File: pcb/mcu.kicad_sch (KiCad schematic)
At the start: 19 parts, among them J15 Conn_01x06_Pin, U20 TM4C123GH6PGEI7, Y2 Crystal_GND24

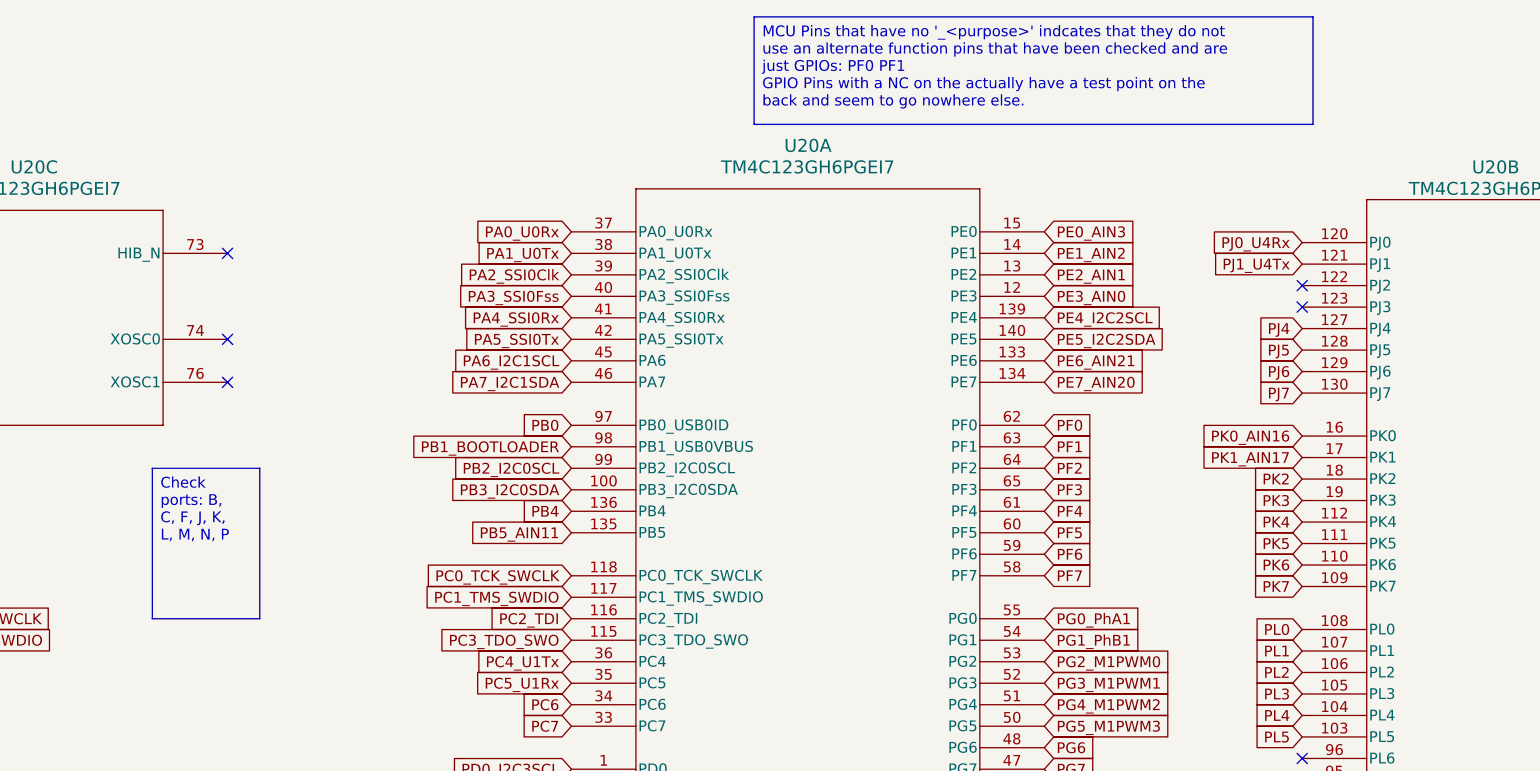
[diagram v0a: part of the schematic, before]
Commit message: Add the last few mystery components to the schematic, update the licence and start on RHSP
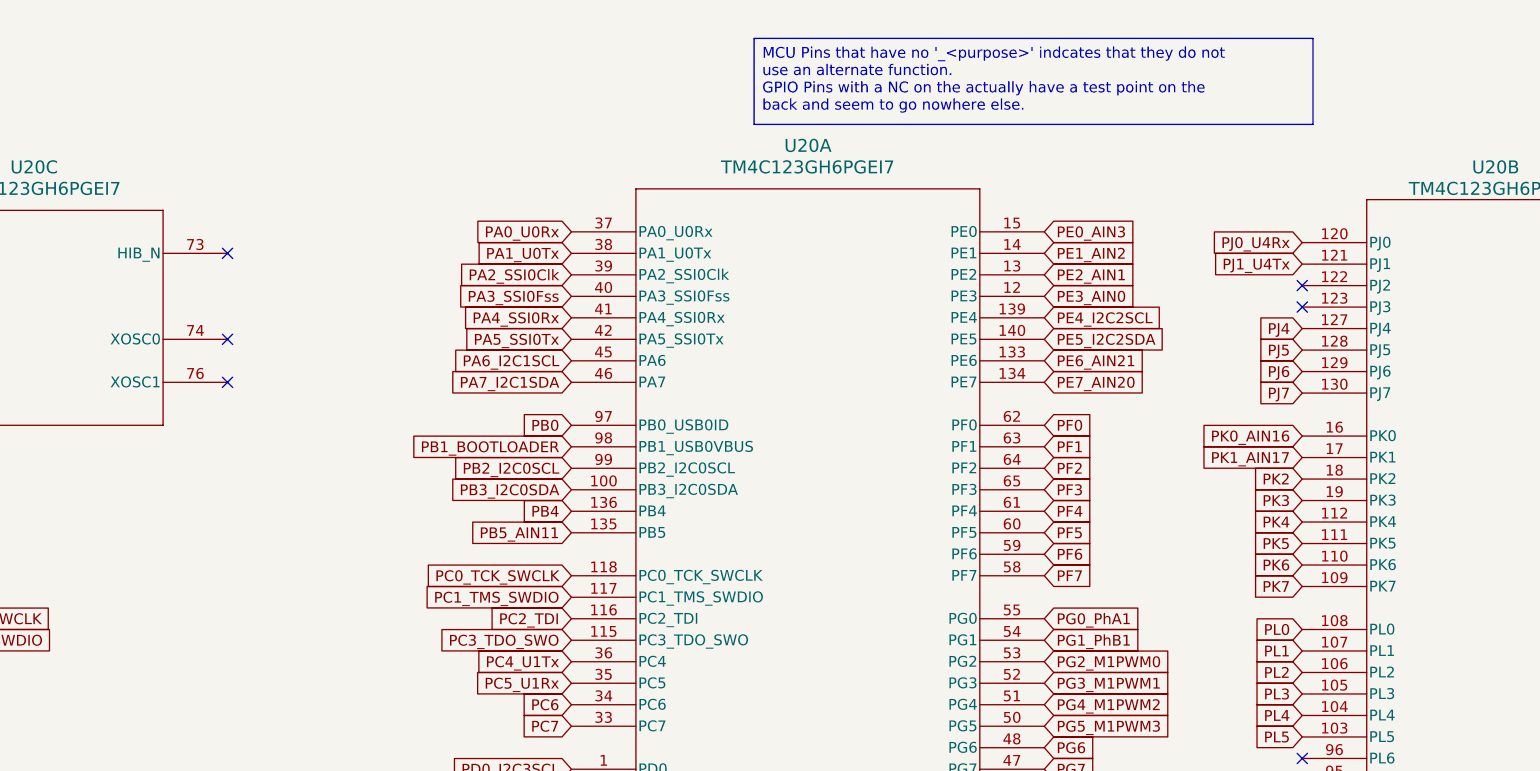
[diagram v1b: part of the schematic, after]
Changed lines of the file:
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@@
 		)
 	)
-	(text_box "MCU Pins that have no '_<purpose>' indcates that they do not use an alternate function pins that have been checked and are just GPIOs: PF0 PF1\nGPIO Pins with a NC on the actually have a test point on the back and seem to go nowhere else."
+	(text_box "MCU Pins that have no '_<purpose>' indcates that they do not use an alternate function.\nGPIO Pins with a NC on the actually have a test point on the back and seem to go nowhere else."
 		(exclude_from_sim no)
-		(at 149.86 2.54 0)
-		(size 66.04 12.7)
+		(at 149.86 5.08 0)
+		(size 66.04 10.16)
 		(margins 0.9525 0.9525 0.9525 0.9525)
 		(stroke
-			(width 0)
-			(type solid)
-		)
-		(fill
-			(type none)
-		)
-		(effects
-			(font
-				(size 1.27 1.27)
-			)
-			(justify left top)
-		)
-	)
-	(text_box "Check ports: B, C, F, J, K, L, M, N, P"
-		(exclude_from_sim no)
-		(at 78.74 55.88 0)
-		(size 12.7 17.78)
-		(margins 0.9525 0.9525 0.9525 0.9525)
-		(stroke

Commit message: Before tear out
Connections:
- net VCC: now also C49.1, U20.77 (VBAT)
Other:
- moved on the sheet: C49
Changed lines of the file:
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@@
 	)
 	(junction
+		(at 267.97 191.77)
+		(diameter 0)
+		(color 0 0 0 0)
+	)
+	(junction
 		(at 27.94 46.99)
 		(diameter 0)
@@
 	(wire
 		(pts
+			(xy 267.97 194.31) (xy 267.97 191.77)
+		)
+		(stroke
+			(width 0)
+			(type default)
+		)
+	)
+	(wire
+		(pts
 			(xy 214.63 152.4) (xy 215.9 152.4)
 		)
@@
 	(wire
 		(pts
+			(xy 280.67 194.31) (xy 278.13 194.31)
+		)
+		(stroke
+			(width 0)
+			(type default)
+		)
+	)
+	(wire
+		(pts
 			(xy 13.97 71.12) (xy 13.97 73.66)
 		)
@@
 	(wire
 		(pts
+			(xy 270.51 189.23) (xy 267.97 189.23)
+		)
+		(stroke
+			(width 0)
+			(type default)
+		)
+	)
+	(wire
+		(pts
 			(xy 45.72 76.2) (xy 27.94 76.2)
 		)
@@
 	(wire
 		(pts
+			(xy 267.97 194.31) (xy 270.51 194.31)
+		)
+		(stroke
+			(width 0)
+			(type default)
+		)
+	)
+	(wire
+		(pts
 			(xy 27.94 71.12) (xy 31.75 71.12)
 		)
@@
 	(wire
 		(pts
+			(xy 267.97 189.23) (xy 267.97 191.77)
+		)
+		(stroke
+			(width 0)
+			(type default)
+		)
+	)
+	(wire
+		(pts
 			(xy 214.63 166.37) (xy 222.25 166.37)
 		)
@@
 	(symbol
 		(lib_id "power:GND")
-		(at 275.59 191.77 90)
+		(at 280.67 194.31 90)
 		(unit 1)
 		(exclude_from_sim no)
@@
 		(fields_autoplaced yes)
 		(property "Reference" "#PWR093"
-			(at 281.94 191.77 0)
+			(at 287.02 194.31 0)
 			(effects
 				(font
@@
 		)
 		(property "Value" "GND"
-			(at 279.4 191.7699 90)
+			(at 284.48 194.3099 90)
 			(effects
 				(font
@@
 		)
 		(property "Footprint" ""
-			(at 275.59 191.77 0)
+			(at 280.67 194.31 0)
 			(effects
 				(font
@@
 		)
 		(property "Datasheet" ""
-			(at 275.59 191.77 0)
+			(at 280.67 194.31 0)
 			(effects
 				(font
@@
 		)
 		(property "Description" "Power symbol creates a global label with name \"GND\" , ground"
-			(at 275.59 191.77 0)
+			(at 280.67 194.31 0)
 			(effects
 				(font
@@
 	(symbol
 		(lib_id "power:VCC")
+		(at 270.51 189.23 270)
+		(unit 1)
+		(exclude_from_sim no)
+		(in_bom yes)
+		(on_board yes)
+		(dnp no)
+		(fields_autoplaced yes)
+		(property "Reference" "#PWR029"
+			(at 266.7 189.23 0)
+			(effects
+				(font
+					(size 1.27 1.27)
+				)
+				(hide yes)
+			)
+		)
+		(property "Value" "VCC"
+			(at 274.32 189.2299 90)
+			(effects
+				(font
+					(size 1.27 1.27)
+				)
+				(justify left)
+			)
+		)
+		(property "Footprint" ""
+			(at 270.51 189.23 0)
+			(effects
+				(font
+					(size 1.27 1.27)
+				)
+				(hide yes)
+			)
+		)
+		(property "Datasheet" ""
+			(at 270.51 189.23 0)
+			(effects
+				(font
+					(size 1.27 1.27)
+				)
+				(hide yes)
+			)
+		)
+		(property "Description" "Power symbol creates a global label with name \"VCC\""
+			(at 270.51 189.23 0)
+			(effects
+				(font
+					(size 1.27 1.27)
+				)
+				(hide yes)
+			)
+		)
+		(pin "1"
+		)
+		(instances
+			(project "pcb"
+				(path "/a3d12dc7-033a-4c99-b909-7e1454b0334e/c2bf59d1-7061-4bc6-a22a-4eecf0a515d0"
+					(reference "#PWR029")
+					(unit 1)
+				)
+			)
+		)
+	)
+	(symbol
+		(lib_id "power:VCC")
 		(at 214.63 166.37 90)
 		(unit 1)
@@
 	(symbol
 		(lib_id "Device:C")
-		(at 271.78 191.77 90)
+		(at 274.32 194.31 90)
 		(unit 1)
 		(exclude_from_sim no)
@@
 		(on_board yes)
 		(dnp no)
-		(fields_autoplaced yes)
 		(property "Reference" "C49"
-			(at 271.78 184.15 90)
+			(at 271.272 195.326 90)
 			(effects
 				(font
@@
 		)
 		(property "Value" "C"
-			(at 271.78 186.69 90)
+			(at 276.098 195.326 90)
 			(effects
 				(font
@@
 		)
 		(property "Footprint" ""
-			(at 275.59 190.8048 0)
+			(at 278.13 193.3448 0)
 			(effects
 				(font
@@
 		)
 		(property "Datasheet" "~"
-			(at 271.78 191.77 0)
+			(at 274.32 194.31 0)
 			(effects
 				(font
@@
 		)
 		(property "Description" "Unpolarized capacitor. Between 2.5 and 4.0 uF"
-			(at 271.78 191.77 0)
+			(at 274.32 194.31 0)
 			(effects
 				(font
